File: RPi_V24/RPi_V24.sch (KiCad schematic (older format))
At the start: 61 parts, among them J1 DB9_Male, J10 Conn_01x03, J11 Conn_01x03, J12 Conn_01x03_Female, J13 Conn_02x04_Odd_Even, J14 Conn_01x03, J15 Conn_01x03, J16 Conn_02x05_Odd_Even, J17 Conn_02x05_Odd_Even, J18 Conn_02x05_Odd_Even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

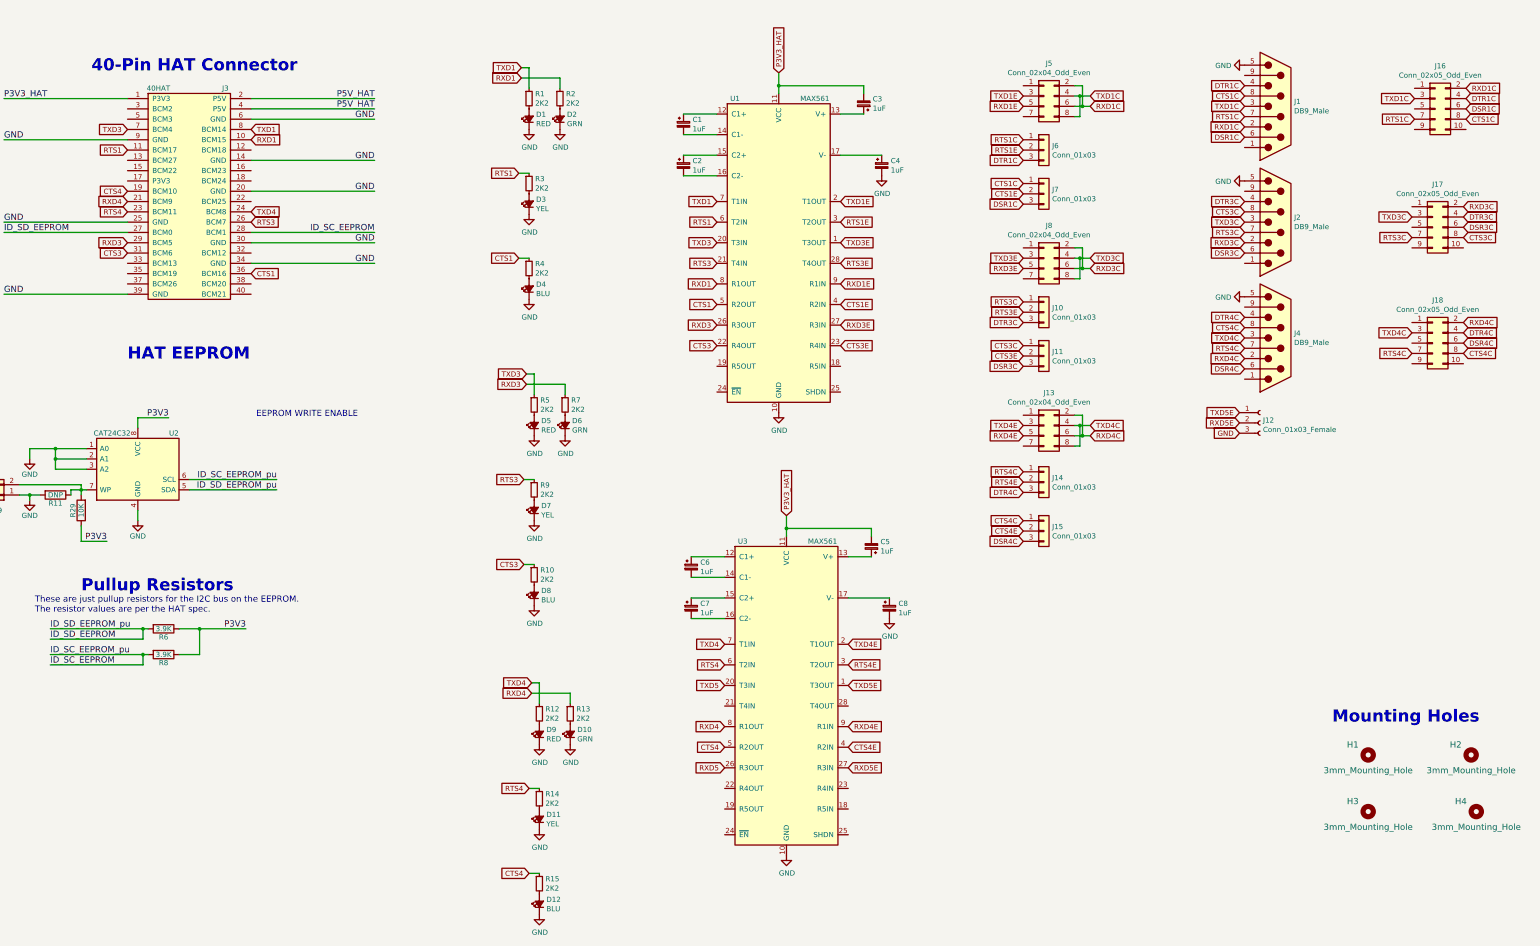
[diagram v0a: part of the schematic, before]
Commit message: Now includes EN and SHDN for the transceivers.
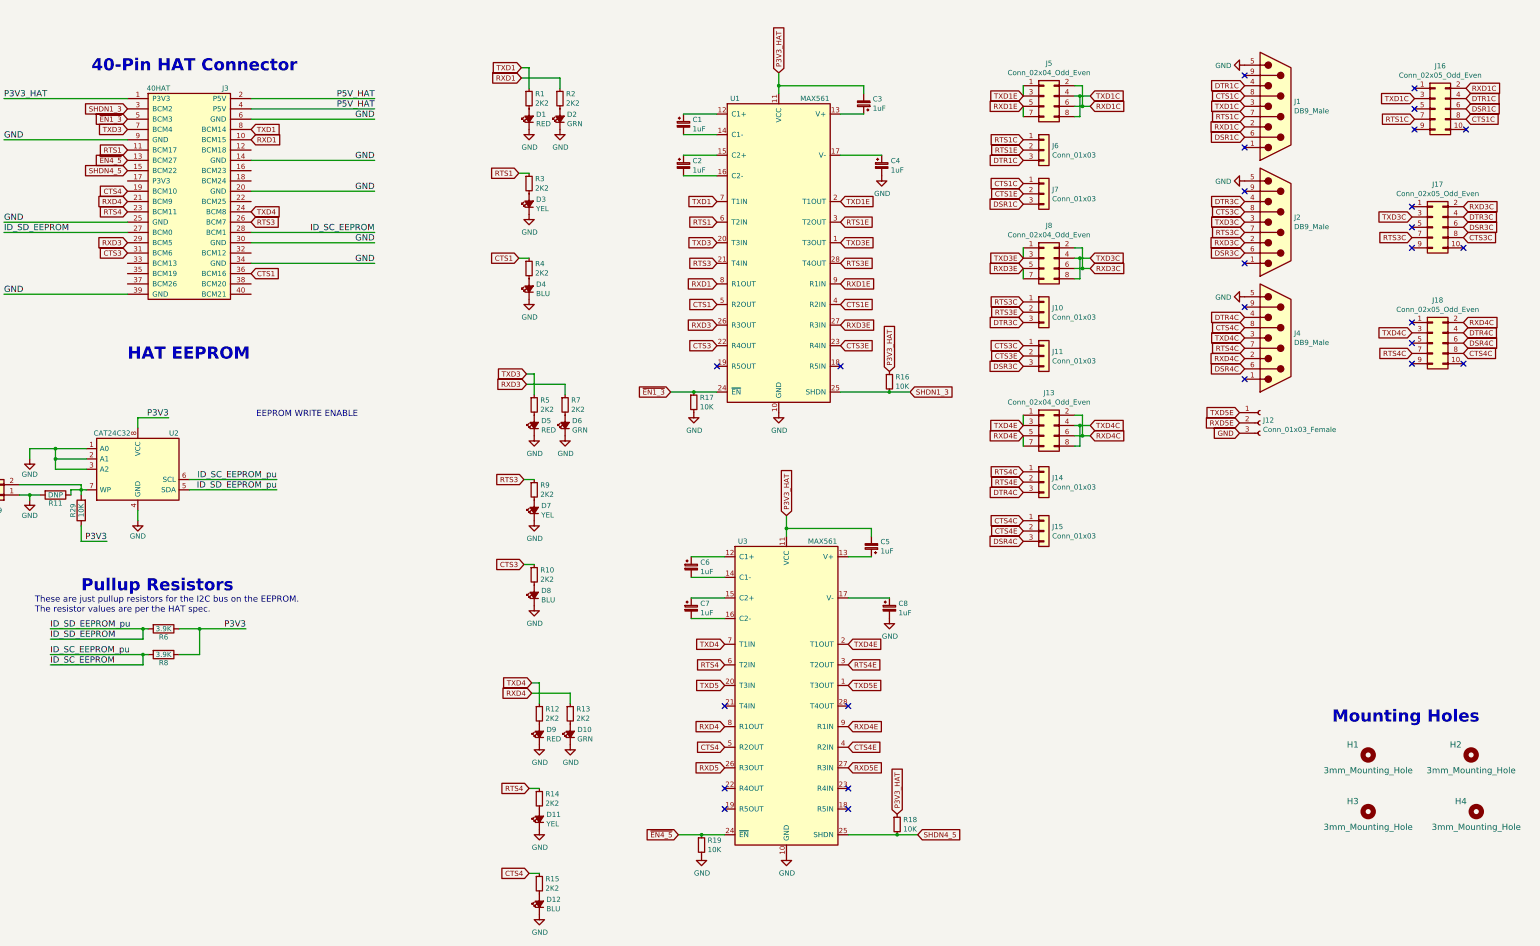
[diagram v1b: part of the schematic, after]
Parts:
- added R16, R17, R18, R19: 10K, Resistor_SMD:R_0402_1005Metric, symbol Device:R_Small
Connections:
- net GND: now also R17.2, R19.2
- net P3V3_HAT: now also R16.1, R18.1
- net RXD1E: now also J5.7 (Pin_7)
- net RXD3E: now also J8.7 (Pin_7)
- net RXD4E: now also J13.7 (Pin_7)
- net TXD1E: now also J5.1 (Pin_1)
- net TXD3E: now also J8.1 (Pin_1)
- net TXD4E: now also J13.1 (Pin_1)
- net ~EN4_5: now reaches J3.13 (BCM27)
- net ~EN4_5: now also U3.24 (~EN), R19.1
- net SHDN4_5: now reaches J3.15 (BCM22)
- net SHDN4_5: now also U3.25 (SHDN), R18.2
- net SHDN1_3: now reaches J3.3 (BCM2)
- net SHDN1_3: now also U1.25 (SHDN), R16.2
- net ~EN1_3: now reaches J3.5 (BCM3)
- net ~EN1_3: now also U1.24 (~EN), R17.1
- no-connect marks 0 -> 26
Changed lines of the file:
@@
 Text GLabel 14975 4625 2    50   Input ~ 0
 DSR4C
-Text GLabel 10700 2325 0    50   Input ~ 0
-RXD1E
-Text GLabel 10700 2225 0    50   Input ~ 0
-TXD1E
 Text GLabel 5825 1950 0    50   Input ~ 0
 TXD1
@@
 Text GLabel 14975 4425 2    50   Input ~ 0
 RXD4C
+Text GLabel 10700 2225 0    50   Input ~ 0
+TXD1E
+Text GLabel 10700 2325 0    50   Input ~ 0
+RXD1E
+Wire Wire Line
+	10700 2125 10700 2225
+Wire Wire Line
+	10700 2325 10700 2425
+Wire Wire Line
+	10700 3700 10700 3800
+Wire Wire Line
+	10700 3900 10700 4000
+Wire Wire Line
+	10700 5325 10700 5425
+Wire Wire Line
+	10700 5525 10700 5625
+NoConn ~ 8925 4850
+NoConn ~ 7725 4850
+NoConn ~ 7800 8150
+NoConn ~ 9000 8150
+NoConn ~ 9000 8950
+NoConn ~ 9000 9150
+NoConn ~ 7800 8950
+NoConn ~ 7800 9150
+NoConn ~ 12850 2025
+NoConn ~ 12850 2725
+NoConn ~ 12850 3150
+NoConn ~ 12850 3850
+NoConn ~ 12850 4275
+NoConn ~ 12850 4975
+NoConn ~ 14475 4425
+NoConn ~ 14475 4625
+NoConn ~ 14475 4825
+NoConn ~ 14975 4825
+NoConn ~ 14975 3700
+NoConn ~ 14475 3700
+NoConn ~ 14475 3500
+NoConn ~ 14475 3300
+NoConn ~ 14500 2150
+NoConn ~ 14500 2350
+NoConn ~ 14500 2550
+NoConn ~ 15000 2550
+Text GLabel 7275 5100 0    50   Input ~ 0
+~EN1_3
+Text GLabel 9600 5100 2    50   Input ~ 0
+SHDN1_3
+Text GLabel 9675 9400 2    50   Input ~ 0
+SHDN4_5
+Text GLabel 7350 9400 0    50   Input ~ 0
+~EN4_5
+$Comp
+L Device:R_Small R19
+U 1 1 61FEEBDB
+P 7575 9500
+F 0 "R19" H 7634 9546 50  0000 L CNN
+F 1 "10K" H 7634 9455 50  0000 L CNN
+F 2 "Resistor_SMD:R_0402_1005Metric" H 7575 9500 50  0001 C CNN
+F 3 "~" H 7575 9500 50  0001 C CNN
+	1    7575 9500
+	1    0    0    -1
+$EndComp
+$Comp
+L power:GND #PWR0120
+U 1 1 61FEF121
+P 7575 9600
+F 0 "#PWR0120" H 7575 9350 50  0001 C CNN
+F 1 "GND" H 7580 9427 50  0000 C CNN
+F 2 "" H 7575 9600 50  0001 C CNN
+F 3 "" H 7575 9600 50  0001 C CNN
+	1    7575 9600
+	1    0    0    -1
+$EndComp
+Wire Wire Line
+	7350 9400 7575 9400
+Connection ~ 7575 9400
+Wire Wire Line
+	7575 9400 7800 9400
+$Comp
+L Device:R_Small R18
+U 1 1 61FF574C
+P 9475 9300
+F 0 "R18" H 9534 9346 50  0000 L CNN
+F 1 "10K" H 9534 9255 50  0000 L CNN
+F 2 "Resistor_SMD:R_0402_1005Metric" H 9475 9300 50  0001 C CNN
+F 3 "~" H 9475 9300 50  0001 C CNN
+	1    9475 9300
+	1    0    0    -1
+$EndComp
+Connection ~ 9475 9400
+Wire Wire Line
+	9475 9400 9675 9400
+Text GLabel 9475 9200 1    50   Input ~ 0
+P3V3_HAT
+Wire Wire Line
+	9000 9400 9475 9400
+$Comp
+L Device:R_Small R17
+U 1 1 62008BC6
+P 7500 5200
+F 0 "R17" H 7559 5246 50  0000 L CNN
+F 1 "10K" H 7559 5155 50  0000 L CNN
+F 2 "Resistor_SMD:R_0402_1005Metric" H 7500 5200 50  0001 C CNN
+F 3 "~" H 7500 5200 50  0001 C CNN
+	1    7500 5200
+	1    0    0    -1
+$EndComp
+$Comp
+L power:GND #PWR0121
+U 1 1 62008BCC
+P 7500 5300
+F 0 "#PWR0121" H 7500 5050 50  0001 C CNN
+F 1 "GND" H 7505 5127 50  0000 C CNN
+F 2 "" H 7500 5300 50  0001 C CNN
+F 3 "" H 7500 5300 50  0001 C CNN
+	1    7500 5300
+	1    0    0    -1
+$EndComp
+Wire Wire Line
+	7275 5100 7500 5100
+Connection ~ 7500 5100
+Wire Wire Line
+	7500 5100 7725 5100
+$Comp
+L Device:R_Small R16
+U 1 1 6202920D
+P 9400 5000
+F 0 "R16" H 9459 5046 50  0000 L CNN
+F 1 "10K" H 9459 4955 50  0000 L CNN
+F 2 "Resistor_SMD:R_0402_1005Metric" H 9400 5000 50  0001 C CNN
+F 3 "~" H 9400 5000 50  0001 C CNN
+	1    9400 5000
+	1    0    0    -1
+$EndComp
+Connection ~ 9400 5100
+Wire Wire Line
+	9400 5100 9600 5100
+Text GLabel 9400 4900 1    50   Input ~ 0
+P3V3_HAT
+Wire Wire Line
+	8925 5100 9400 5100
+Text GLabel 2000 2450 0    50   Input ~ 0
+~EN1_3
+Text GLabel 2000 2350 0    50   Input ~ 0
+SHDN1_3
+Text GLabel 2000 2850 0    50   Input ~ 0
+~EN4_5
+Text GLabel 2000 2950 0    50   Input ~ 0
+SHDN4_5
 $EndSCHEMATC
